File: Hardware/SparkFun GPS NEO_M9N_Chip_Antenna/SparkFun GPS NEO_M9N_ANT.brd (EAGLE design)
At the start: 40.6 x 33 mm, 89 parts, among them J2 Qwiic Right Angle, J4 Qwiic Right Angle, U1 U-BLOX_NEO-M9N, U2 3.3V, Y1 GPS_CHIP_ANTENNAW3011

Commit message: Fixes an air wire and wire stub
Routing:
- net SDA/!CS: track 88.8 -> 88.2 mm
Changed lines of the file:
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@@
 <layer number="27" name="tValues" color="7" fill="1" visible="no" active="yes"/>
 <layer number="28" name="bValues" color="7" fill="1" visible="no" active="yes"/>
-<layer number="29" name="tStop" color="7" fill="3" visible="yes" active="yes"/>
+<layer number="29" name="tStop" color="7" fill="3" visible="no" active="yes"/>
 <layer number="30" name="bStop" color="7" fill="6" visible="no" active="yes"/>
-<layer number="31" name="tCream" color="7" fill="4" visible="yes" active="yes"/>
+<layer number="31" name="tCream" color="7" fill="4" visible="no" active="yes"/>
 <layer number="32" name="bCream" color="7" fill="5" visible="no" active="yes"/>
 <layer number="33" name="tFinish" color="6" fill="3" visible="no" active="yes"/>
@@
 <layer number="45" name="Holes" color="7" fill="1" visible="yes" active="yes"/>
 <layer number="46" name="Milling" color="3" fill="1" visible="no" active="yes"/>
-<layer number="47" name="Measures" color="7" fill="1" visible="yes" active="yes"/>
+<layer number="47" name="Measures" color="7" fill="1" visible="no" active="yes"/>
 <layer number="48" name="Document" color="7" fill="1" visible="no" active="yes"/>
 <layer number="49" name="Reference" color="13" fill="1" visible="yes" active="yes"/>
@@
 <layer number="115" name="ReferenceISLANDS" color="7" fill="1" visible="no" active="no"/>
 <layer number="116" name="Patch_BOT" color="9" fill="4" visible="no" active="no"/>
-<layer number="117" name="PM_Ref" color="26" fill="1" visible="yes" active="yes"/>
+<layer number="117" name="PM_Ref" color="26" fill="1" visible="no" active="yes"/>
 <layer number="118" name="Rect_Pads" color="7" fill="1" visible="no" active="no"/>
-<layer number="119" name="PF_Ref" color="31" fill="1" visible="yes" active="yes"/>
-<layer number="120" name="WFL_Ref" color="25" fill="1" visible="yes" active="yes"/>
+<layer number="119" name="PF_Ref" color="31" fill="1" visible="no" active="yes"/>
+<layer number="120" name="WFL_Ref" color="25" fill="1" visible="no" active="yes"/>
 <layer number="121" name="_tsilk" color="7" fill="1" visible="no" active="no"/>
 <layer number="122" name="_bsilk" color="7" fill="1" visible="no" active="no"/>
@@
 <wire x1="6.096" y1="20.32" x2="6.35" y2="20.066" width="0.1524" layer="1"/>
 <wire x1="6.35" y1="20.066" x2="6.35" y2="18.7706" width="0.1524" layer="1"/>
-<wire x1="5.08" y1="15.0956" x2="5.723" y2="15.0956" width="0.1524" layer="1"/>
 <wire x1="5.08" y1="15.0956" x2="3.9798" y2="15.0956" width="0.1524" layer="1"/>
 <wire x1="3.9798" y1="15.0956" x2="3.683" y2="15.3924" width="0.1524" layer="1"/>
 <wire x1="3.683" y1="15.3924" x2="3.683" y2="18.2626" width="0.1524" layer="1"/>
-<wire x1="5.08" y1="15.0956" x2="6.2056" y2="15.0956" width="0.1524" layer="1"/>
 <wire x1="8.6106" y1="17.5006" x2="9.31" y2="17.5006" width="0.1524" layer="1"/>
-<wire x1="6.2056" y1="15.0956" x2="8.6106" y2="17.5006" width="0.1524" layer="1"/>
+<wire x1="8.6106" y1="17.5006" x2="6.2056" y2="15.0956" width="0.1524" layer="1"/>
+<wire x1="6.2056" y1="15.0956" x2="5.08" y2="15.0956" width="0.1524" layer="1"/>
 </signal>
 <signal name="!RESET">

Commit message: Removes local eagle library and replaces part from that library with part from SparkFun Eagle Library
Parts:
- U1: device gps:NEO-M9N -> SparkFun-GPS:NEO-M9N
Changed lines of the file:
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@@
 <layer number="115" name="ReferenceISLANDS" color="7" fill="1" visible="no" active="no"/>
 <layer number="116" name="Patch_BOT" color="9" fill="4" visible="no" active="no"/>
-<layer number="117" name="PM_Ref" color="26" fill="1" visible="no" active="yes"/>
+<layer number="117" name="PM_Ref" color="26" fill="1" visible="yes" active="yes"/>
 <layer number="118" name="Rect_Pads" color="7" fill="1" visible="no" active="no"/>
-<layer number="119" name="PF_Ref" color="31" fill="1" visible="no" active="yes"/>
-<layer number="120" name="WFL_Ref" color="25" fill="1" visible="no" active="yes"/>
+<layer number="119" name="PF_Ref" color="31" fill="1" visible="yes" active="yes"/>
+<layer number="120" name="WFL_Ref" color="25" fill="1" visible="yes" active="yes"/>
 <layer number="121" name="_tsilk" color="7" fill="1" visible="no" active="no"/>
 <layer number="122" name="_bsilk" color="7" fill="1" visible="no" active="no"/>
@@
 <element name="U$37" library="buzzard_labels (36)" package="TX#MISO1" value="" x="31.7754" y="24.0284" smashed="yes" rot="MR90"/>
 <element name="LOGO2" library="SparkFun-Aesthetics" package="SFE_LOGO_NAME_FLAME_.1" value="SFE_LOGO_NAME_FLAME.1_INCH" x="20.193" y="20.6756" smashed="yes" rot="MR0"/>
-<element name="U1" library="gps" package="NEO-M9N" value="U-BLOX_NEO-M9N" x="20.32" y="16.2306" smashed="yes">
+<element name="U1" library="SparkFun-GPS" package="NEO-M9N" value="U-BLOX_NEO-M9N" x="20.32" y="16.2306" smashed="yes">
 <attribute name="NAME" x="14.22" y="24.7306" size="0.508" layer="25"/>
 <attribute name="PROD_ID" value="IC-14651" x="20.32" y="16.2306" size="1.778" layer="27" display="off"/>

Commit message: Updates libs, adds SMA connector and rf bias circuit
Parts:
- removed Y1: GPS_CHIP_ANTENNAW3011, SparkFun-GPS:W3011
- added C1: 47pF, SparkFun-Capacitors:0402
- added E1: ANTENNA-GROUNDEDEDGE_RPSMA_SMD, SparkFun-RF:SMA-EDGE-SMD
- added FB1: FERRITE_BEAD-120_OHM-0402, SparkFun-Coils:0402
- added R14: 33, SparkFun-Resistors:0402
- J3: device SparkFun-Connectors:USB-C-16P -> SparkFun-Connectors:USB-C-16P-2LAYER-PADS
- U1: device SparkFun-GPS:NEO-M9N -> SparkFun-GPS:NEO-M9N/M8T/M8U
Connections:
- new net N$3: C1.1, FB1.2, R14.1
- net GND: now also C1.2, E1.GND@0, E1.GND@1; no longer Y1.2, Y1.3
- net GPS_ANT1: now also E1.SIG, FB1.1; no longer Y1.1
- net SHLD: no longer J3.SHLD5, J3.SHLD6, J3.SHLD7, J3.SHLD8
- net VCC_RF: now also R14.2
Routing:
- net USB_D-: track 3.36 -> 4.35 mm
- net GND: vias 173 -> 167

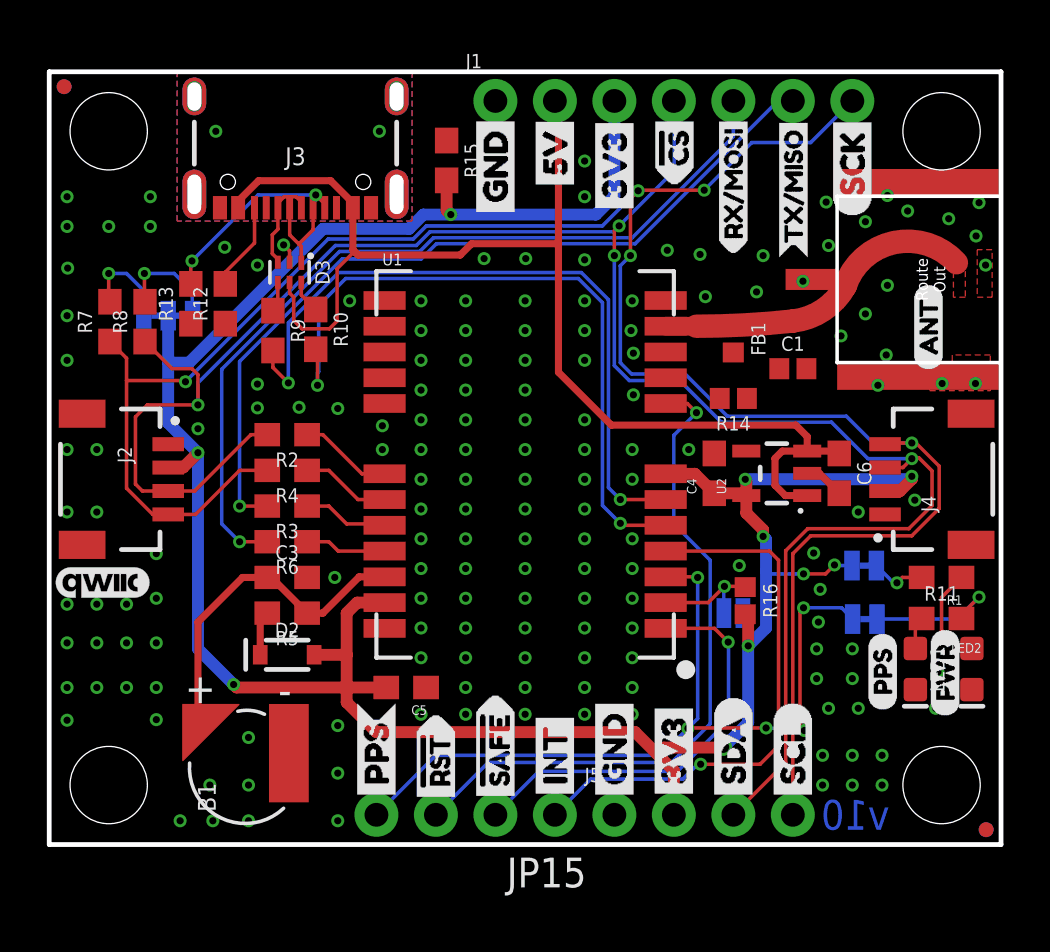
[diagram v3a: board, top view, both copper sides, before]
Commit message: Routed updates USB footprint and SMA connector with its RF circuitry
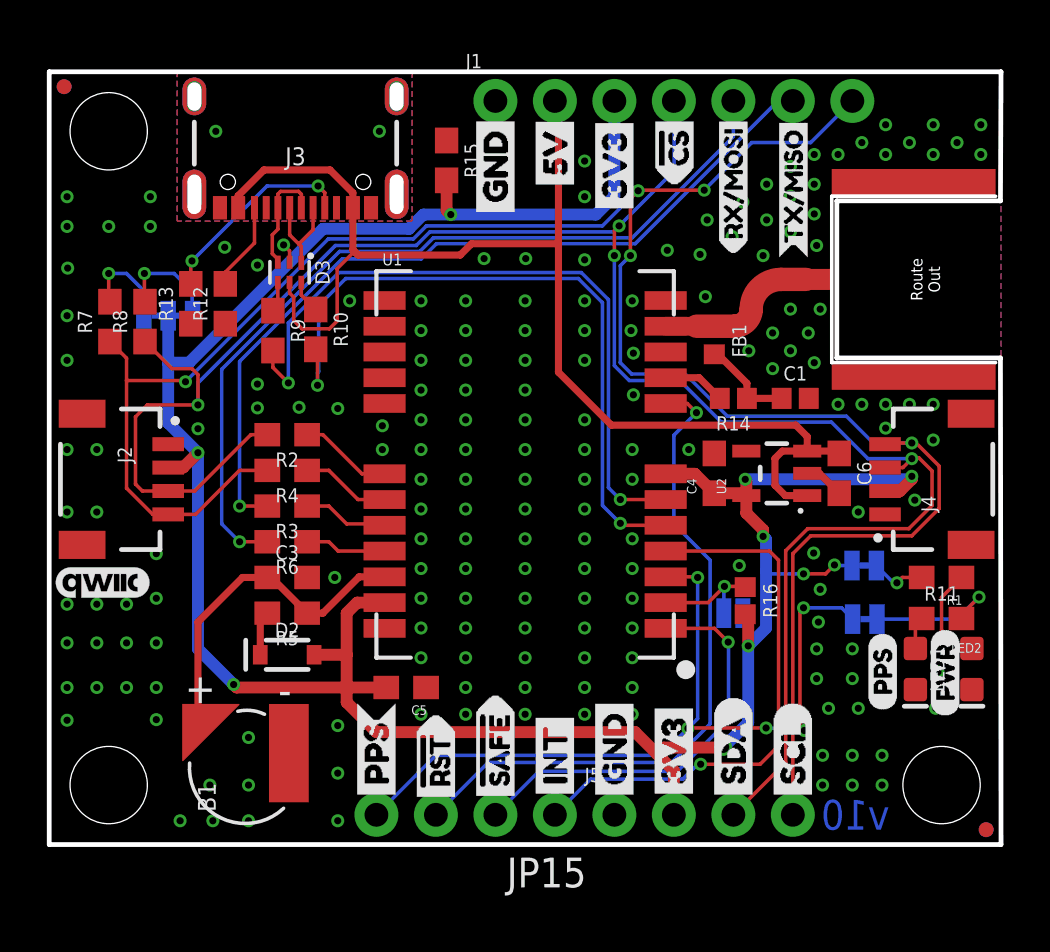
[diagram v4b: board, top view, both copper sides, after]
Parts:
- removed JP41: STAND-OFF, SparkFun:STAND-OFF
- removed U$13: (no value), ANT:ANT0
- removed U$38, U$41: (no value), Labels:SCK-(]-04
- moved C1 1.27 mm to (31.9, 19.1)
- moved FB1 0.82 mm to (28.4, 21.5)
- moved E1 0.23 mm to (40.4, 24.1)
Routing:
- net GPS_ANT1: track 13.0 -> 6.82 mm
- net N$3: track 0.00 -> 4.03 mm
- net VCC_RF: track 0.00 -> 2.67 mm
- net 5V: track 53.8 -> 54.6 mm
- net USB_D+: track 4.18 -> 4.78 mm
- net N$9: track 8.16 -> 8.76 mm
- net GND: vias 167 -> 186
- removed copper zone on layer 1, net GPS_ANT1
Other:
- outline, holes or cut-outs redrawn
